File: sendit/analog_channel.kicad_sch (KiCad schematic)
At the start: 22 parts, among them J2 Conn_02x05_Odd_Even, J26 Conn_01x03, J29 JUMPER, J3 Conn_02x05_Odd_Even, J41 JUMPER, J49 JUMPER, J57 JUMPER

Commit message: switch to test points with drilled holes.
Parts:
- TP1: footprint TestPoint:TestPoint_Pad_D1.0mm -> TestPoint:TestPoint_THTPad_D1.0mm_Drill0.5mm
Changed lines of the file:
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@@
 			)
 		)
-		(property "Footprint" "TestPoint:TestPoint_Pad_D1.0mm"
+		(property "Footprint" "TestPoint:TestPoint_THTPad_D1.0mm_Drill0.5mm"
 			(at 62.23 101.6 0)
 			(effects

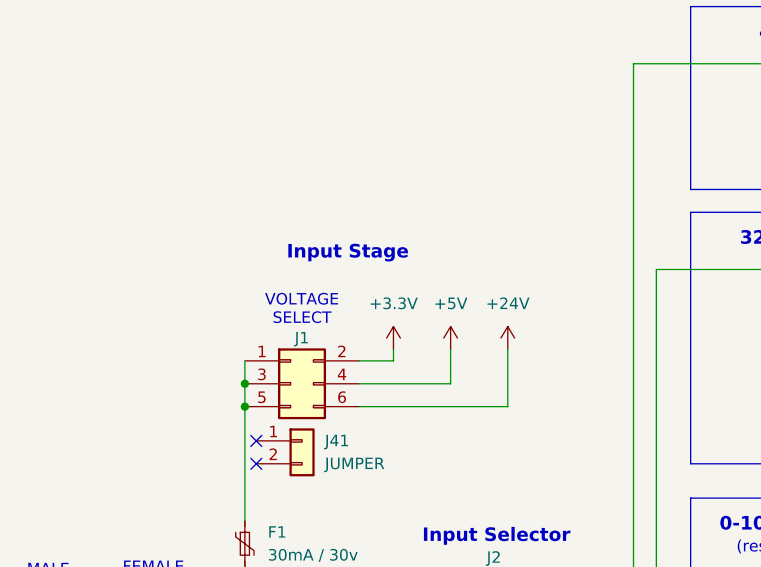
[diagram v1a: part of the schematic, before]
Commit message: added alert lines
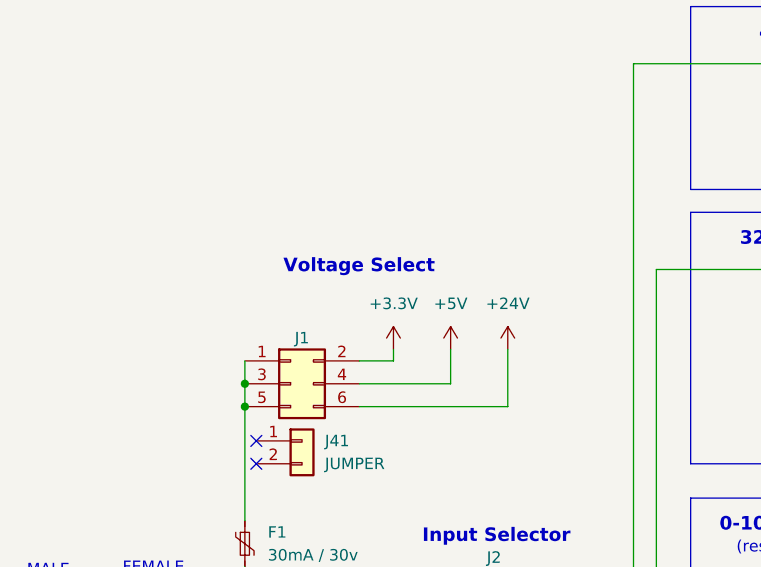
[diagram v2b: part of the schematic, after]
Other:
- note added: "Voltage Select"
- note removed: "Input Stage"
- note removed: "VOLTAGE SELECT"
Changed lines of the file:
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@@
 		)
 	)
-	(text "Input Stage"
+	(text "Voltage Select"
 		(exclude_from_sim no)
-		(at 59.69 59.182 0)
+		(at 60.96 60.706 0)
 		(effects
 			(font
@@
 			)
 		)
-	)
-	(text "VOLTAGE\nSELECT"
-		(exclude_from_sim no)
-		(at 54.61 65.532 0)
-		(effects
-			(font
-				(size 1.27 1.27)
-			)
-		)

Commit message: big schematic rework for Rev B
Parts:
- removed J29: JUMPER, symbol Connector_Generic:Conn_01x02
- removed R4: 1k 0.1%, Resistor_SMD:R_0603_1608Metric, symbol Device:R_Small_US
- added D17: PESD3V3L1BA,115, Diode_SMD:D_SOD-323, symbol Device:D_TVS
- J3: renamed from J1; footprint Connector_PinHeader_2.54mm:PinHeader_2x03_P2.54mm_Vertical -> Connector_PinHeader_2.54mm:PinHeader_2x04_P2.54mm_Vertical; symbol Connector_Generic:Conn_02x03_Odd_Even -> Connector_Generic:Conn_02x04_Odd_Even; LCSC C225518 -> C225519
- renumbered INPUT1 to INPUT2, J26 to J2, J41 to J4, J2 to J5, J49 to J6, J3 to J7, J57 to J8, R5 to R4, R6 to R5, R7 to R6, R8 to R7
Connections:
- net GND: now also D17.1 (A1)
- net at F1.1, J3.1 (Pin_1), J3.3 (Pin_3)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: now also J3.7 (Pin_7)
- net at J7.10 (Pin_10), J7.2 (Pin_2), J7.4 (Pin_4)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: now also D17.2 (A2)
- net +3.3V renamed +3.3VADC
- new net EXTERN: J3.8 (Pin_8)
- no-connect marks 11 -> 9
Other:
- note added: "Passthrough"
- note removed: "0-1000 ohm Resistance Sensor"
- moved on the sheet: D1, J4, J6, J8, R7, TP2

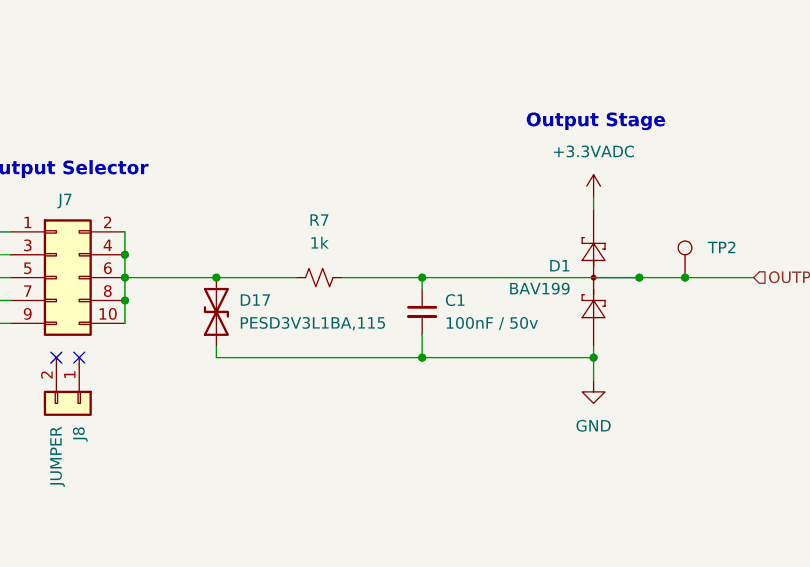
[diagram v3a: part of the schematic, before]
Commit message: brought over the latest esp32-s3 schematic
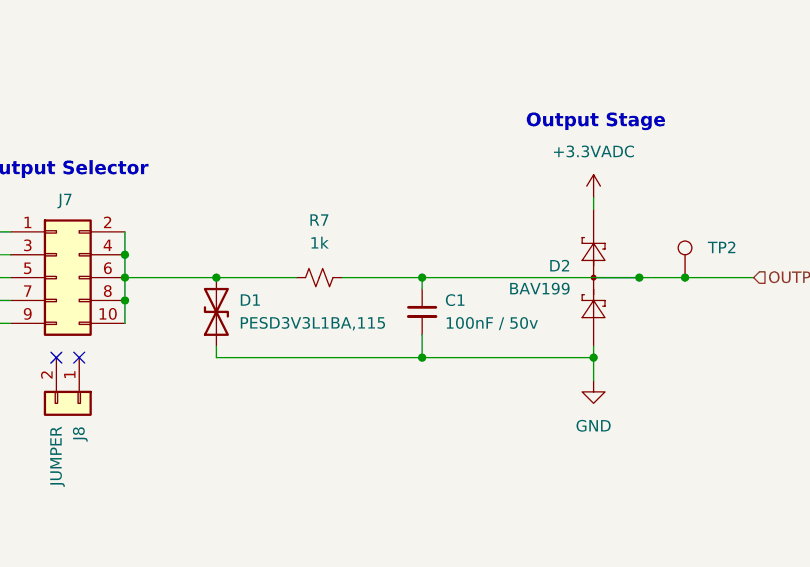
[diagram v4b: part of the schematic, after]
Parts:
- renumbered D17 to D1, D1 to D2

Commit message: bom and placement looking good.
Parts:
- J3, J5, J7: Rotation Offset (none) -> 90

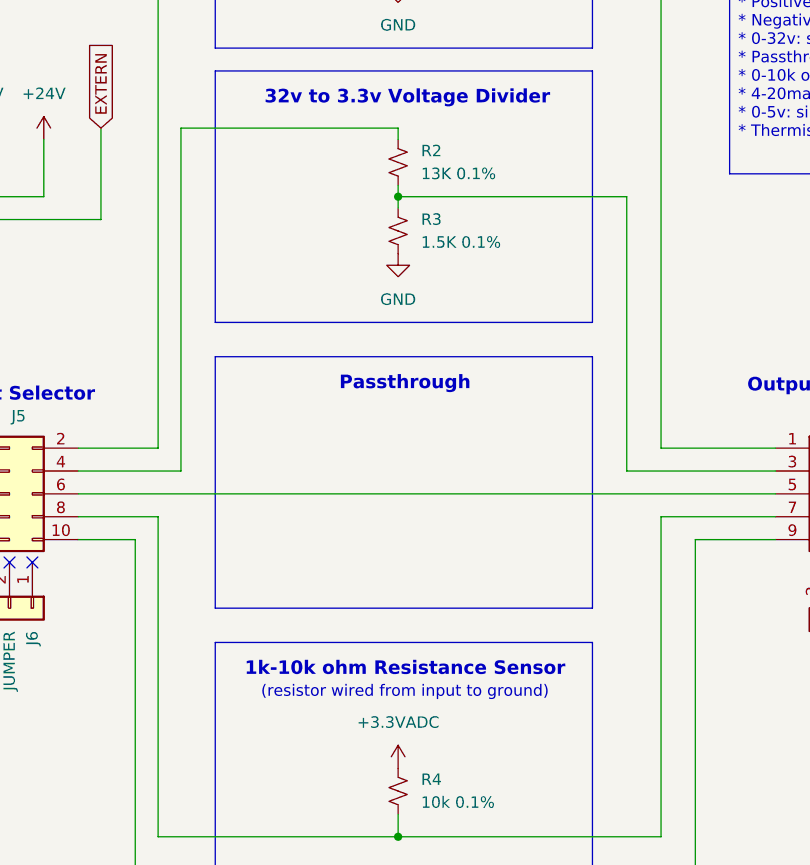
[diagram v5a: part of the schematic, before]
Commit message: some final resistor value tweaking
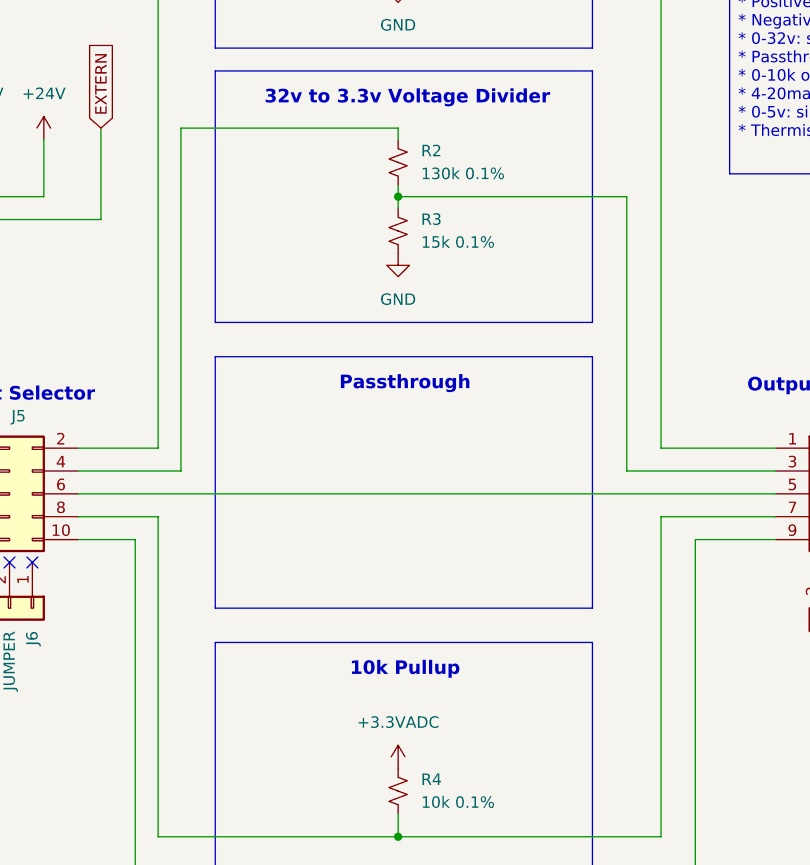
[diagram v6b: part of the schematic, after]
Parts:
- R2: value 13K 0.1% -> 130k 0.1%; LCSC C861121 -> (none)
- R3: value 1.5K 0.1% -> 15k 0.1%; LCSC C705741 -> (none)
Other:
- note added: "10k Pullup"
- note removed: "(resistor wired from input to ground)"
- note removed: "1k-10k ohm Resistance Sensor"
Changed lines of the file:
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@@
 		)
 	)
-	(text "1k-10k ohm Resistance Sensor"
+	(text "10k Pullup"
 		(exclude_from_sim no)
 		(at 118.872 121.158 0)
@@
 				(thickness 0.4)
 				(bold yes)
-			)
-		)
-	)
-	(text "(resistor wired from input to ground)"
-		(exclude_from_sim no)
-		(at 118.872 123.698 0)
-		(effects
-			(font
-				(size 1.27 1.27)
 			)
 		)
@@
 			)
 		)
-		(property "Value" "1.5K 0.1%"
+		(property "Value" "15k 0.1%"
 			(at 120.65 73.66 0)
 			(effects
@@
 			)
 		)
-		(property "LCSC" "C705741"
+		(property "LCSC" ""
 			(at 118.11 72.39 0)
 			(effects
@@
 			)
 		)
-		(property "Value" "13K 0.1%"
+		(property "Value" "130k 0.1%"
 			(at 120.65 66.0399 0)
 			(effects
@@
 			)
 		)
-		(property "LCSC" "C861121"
+		(property "LCSC" ""
 			(at 118.11 64.77 0)
 			(effects

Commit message: cleaning up schematics a bit for design review
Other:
- title: (none) -> https://github.com/hoeken/sendit
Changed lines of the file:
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@@
 	(generator_version "9.0")
 	(paper "A4")
+	(title_block
+		(title "https://github.com/hoeken/sendit")
+		(date "2025-08-28")
+		(rev "B")
+	)
 	(rectangle
 		(start 97.79 31.75)

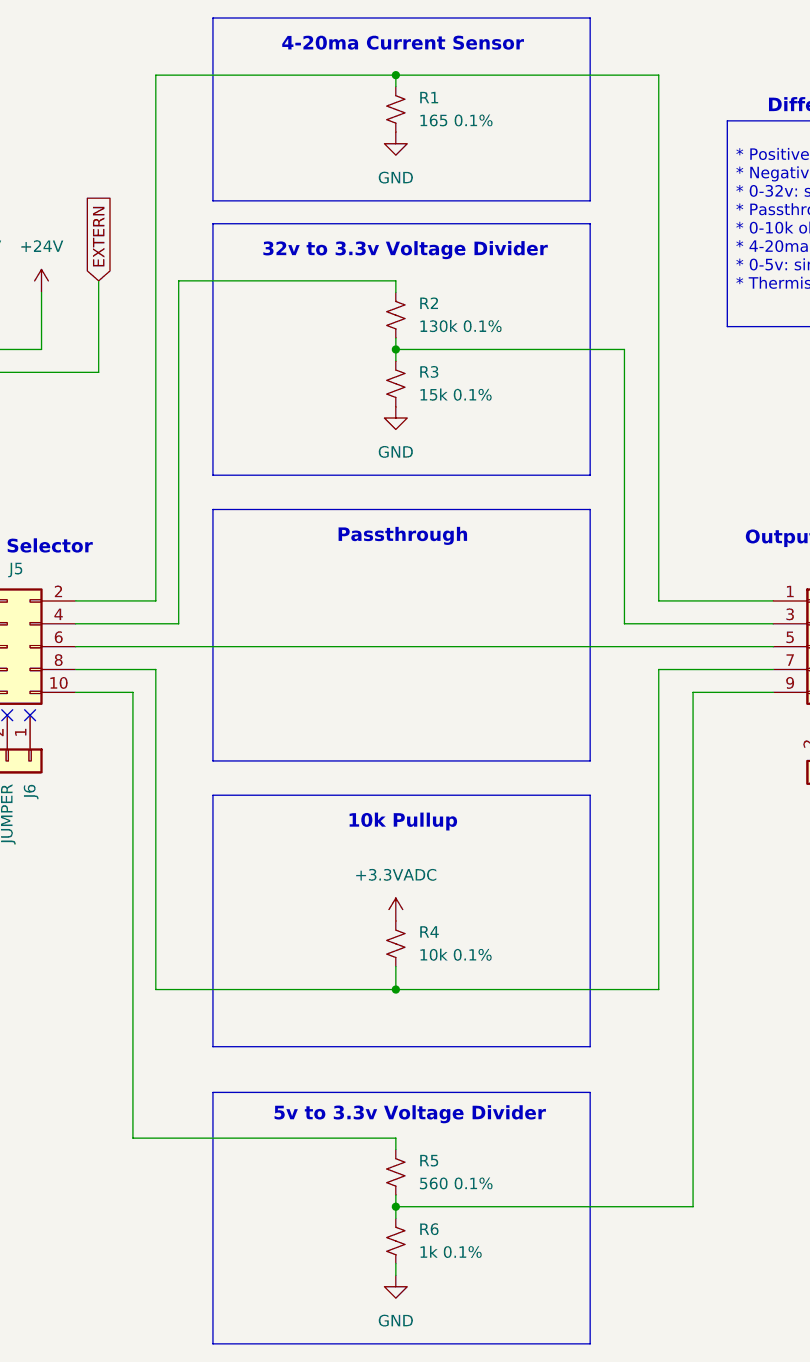
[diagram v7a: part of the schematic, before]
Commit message: started work on the rev c schematic
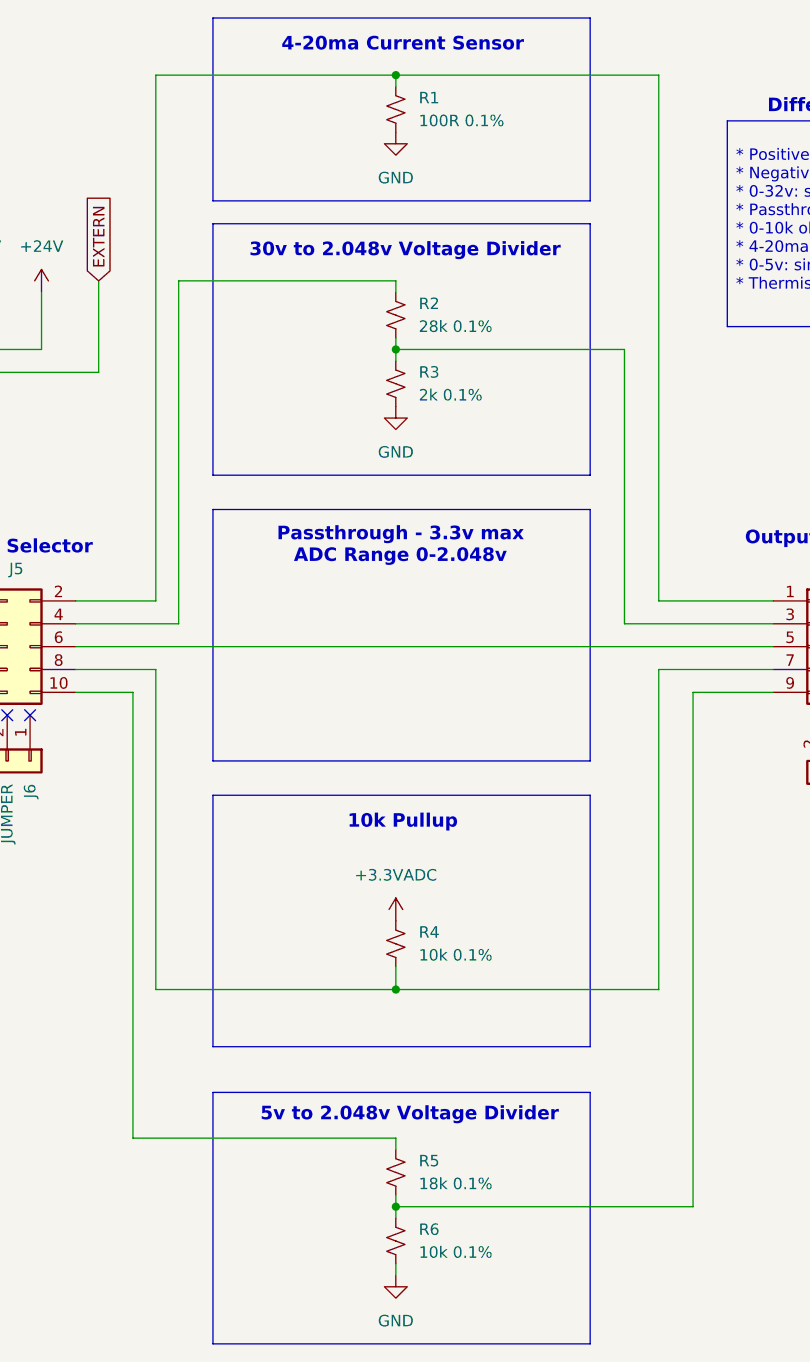
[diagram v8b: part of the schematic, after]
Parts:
- R1: value 165 0.1% -> 100R 0.1%; LCSC C870446 -> C728670
- R2: value 130k 0.1% -> 28k 0.1%
- R3: value 15k 0.1% -> 2k 0.1%
- R4: LCSC C95204 -> C860067
- R5: value 560 0.1% -> 18k 0.1%; LCSC C860442 -> C860169
- R6: value 1k 0.1% -> 10k 0.1%; LCSC C110776 -> C860067
- TP1, TP2: footprint TestPoint:TestPoint_THTPad_D1.0mm_Drill0.5mm -> TestPoint:TestPoint_THTPad_D1.5mm_Drill0.7mm
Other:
- note added: "30v to 2.048v Voltage Divider"
- note added: "5v to 2.048v Voltage Divider"
- note added: "Passthrough - 3.3v max ADC Range 0-2.048v"
- note removed: "32v to 3.3v Voltage Divider"
- note removed: "5v to 3.3v Voltage Divider"
- note removed: "Passthrough"
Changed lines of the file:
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@@
 		(title "https://github.com/hoeken/sendit")
 		(date "2025-08-28")
-		(rev "B")
+		(rev "C")
 	)
 	(rectangle
@@
 		)
 	)
-	(text "32v to 3.3v Voltage Divider"
+	(text "30v to 2.048v Voltage Divider"
 		(exclude_from_sim no)
 		(at 119.126 57.658 0)
@@
 		)
 	)
-	(text "Passthrough"
+	(text "Passthrough - 3.3v max\nADC Range 0-2.048v"
 		(exclude_from_sim no)
-		(at 118.872 89.408 0)
+		(at 118.618 90.424 0)
 		(effects
 			(font
@@
 		)
 	)
-	(text "5v to 3.3v Voltage Divider"
+	(text "5v to 2.048v Voltage Divider"
 		(exclude_from_sim no)
 		(at 119.634 153.67 0)
@@
 			)
 		)
-		(property "LCSC" "C95204"
+		(property "LCSC" "C860067"
 			(at 118.11 134.62 0)
 			(effects
@@
 			)
 		)
-		(property "Value" "15k 0.1%"
+		(property "Value" "2k 0.1%"
 			(at 120.65 73.66 0)
 			(effects
@@
 			)
 		)
-		(property "Value" "1k 0.1%"
+		(property "Value" "10k 0.1%"
 			(at 120.65 168.91 0)
 			(effects
@@
 			)
 		)
-		(property "LCSC" "C110776"
+		(property "LCSC" "C860067"
 			(at 118.11 167.64 0)
 			(effects
@@
 			)
 		)
-		(property "Value" "130k 0.1%"
+		(property "Value" "28k 0.1%"
 			(at 120.65 66.0399 0)
 			(effects
@@
 			)
 		)
-		(property "Value" "165 0.1%"
+		(property "Value" "100R 0.1%"
 			(at 120.65 43.18 0)
 			(effects
@@
 			)
 		)
-		(property "LCSC" "C870446"
+		(property "LCSC" "C728670"
 			(at 118.11 41.91 0)
 			(effects
@@
 			)
 		)
-		(property "Value" "560 0.1%"
+		(property "Value" "18k 0.1%"
 			(at 120.65 161.2899 0)
 			(effects
@@
 			)
 		)
-		(property "LCSC" "C860442"
+		(property "LCSC" "C860169"
 			(at 118.11 160.02 0)
 			(effects
@@
 			)
 		)
-		(property "Footprint" "TestPoint:TestPoint_THTPad_D1.0mm_Drill0.5mm"
+		(property "Footprint" "TestPoint:TestPoint_THTPad_D1.5mm_Drill0.7mm"
 			(at 62.23 101.6 0)
 			(effects
@@
 			)
 		)
-		(property "Footprint" "TestPoint:TestPoint_THTPad_D1.0mm_Drill0.5mm"
+		(property "Footprint" "TestPoint:TestPoint_THTPad_D1.5mm_Drill0.7mm"
 			(at 240.03 101.6 0)
 			(effects
